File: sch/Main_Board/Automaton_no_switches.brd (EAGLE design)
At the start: 100 x 80 mm, 16 parts, among them IC1 74LS595D, IC2 74LS595D, IC3 74LS595D, IC4 74LS595D, J1 POWER_JACKPTH

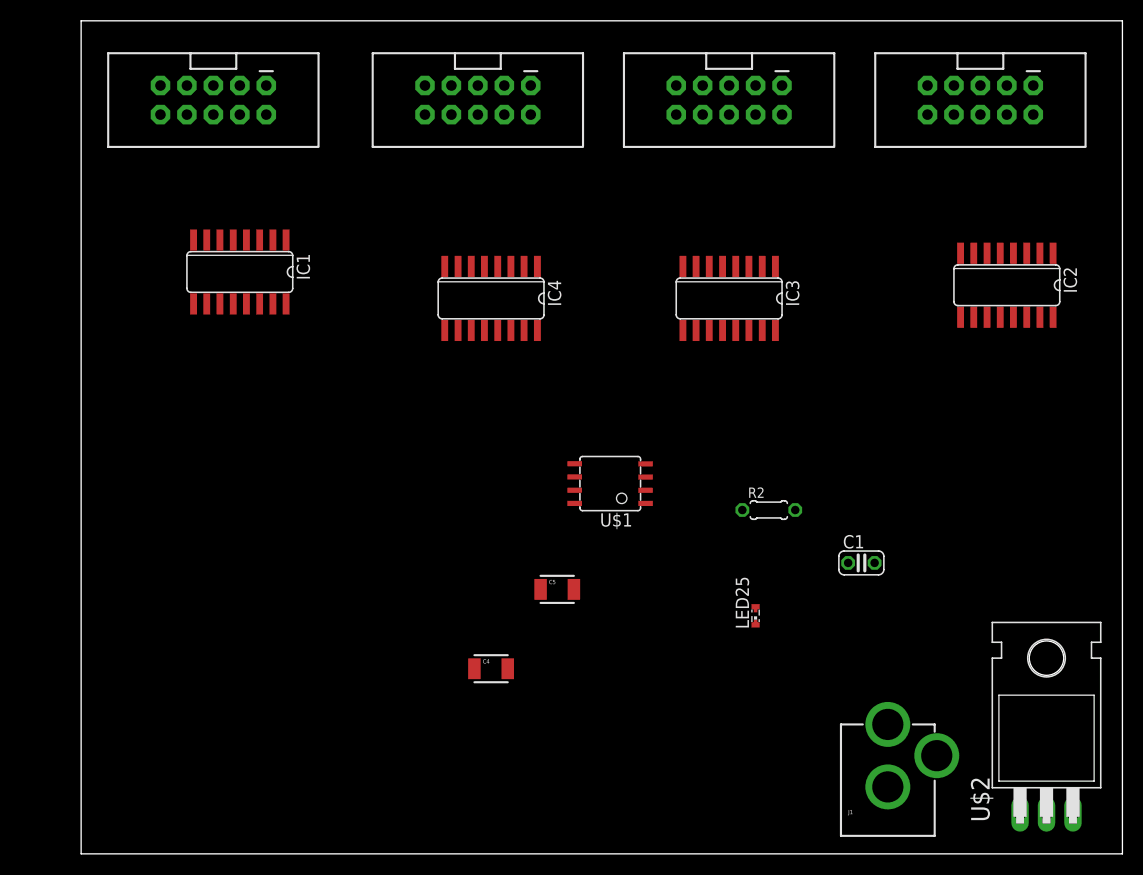
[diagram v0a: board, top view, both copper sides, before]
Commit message: More schematic work.  Make a potentially working board for the main automaton circuit.
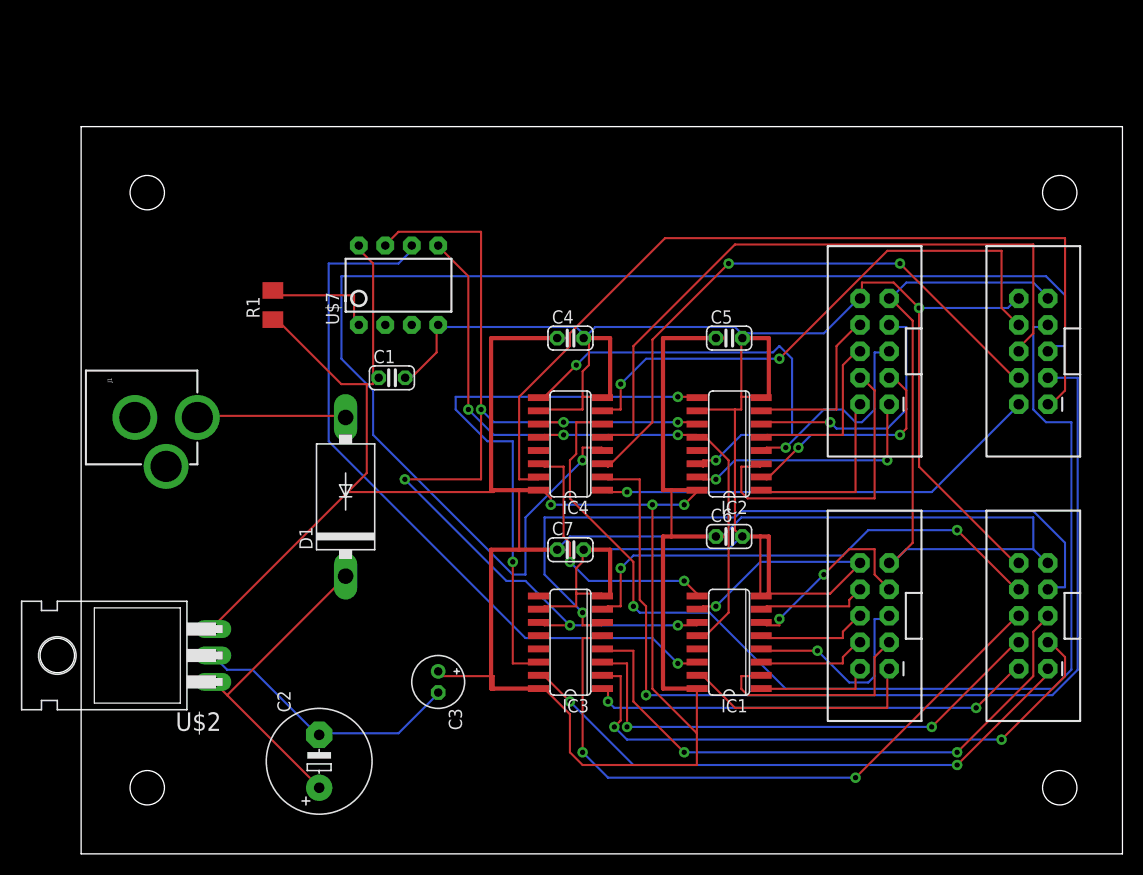
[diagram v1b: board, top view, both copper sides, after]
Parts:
- removed LED25: (no value), led:SMARTLED-TTW
- removed R2: 330, resistor:0204/5
- removed U$1: TINY13-20SU, MyAtmel:8S2
- added C2: 100uf, rcl:E5-10,5
- added C3: 10uf, rcl:E2-5
- added C6, C7: 0.1uf, resistor:C025-024X044
- added D1: 1N5400, diode:DO201-15
- added JP1, JP2, JP3, JP4: STAND-OFF, SparkFun-Electromechanical:STAND-OFF
- added R1: 10k, resistor:M1206
- added U$7: ATTINY85DIP8, *Personal Library:DIP08
- C4: value 10uf -> 0.1uf; device SparkFun:1210 -> resistor:C025-024X044
- C5: value 100uf -> 0.1uf; device SparkFun:1210 -> resistor:C025-024X044
- moved J1 90.9 mm to (-2.54, 41.9), turned to 270 degrees
- moved U$2 90.3 mm to (2.54, 19.1), turned to 90 degrees
- moved U$6 80.5 mm to (76.2, 22.9), turned to 180 degrees
- moved IC1 58.9 mm to (62.2, 20.3), turned to 90 degrees
- moved U$5 58.5 mm to (91.4, 48.3), turned to 180 degrees
- moved U$3 57.5 mm to (91.4, 22.9), turned to 180 degrees
- moved C1 48.5 mm to (29.8, 45.7)
- moved IC3 36.4 mm to (47.0, 20.3), turned to 90 degrees
- moved C4 32.7 mm to (47.0, 49.5)
- moved IC2 30.7 mm to (62.2, 39.4), turned to 90 degrees
- moved C5 29.2 mm to (62.2, 49.5)
- moved U$4 26.2 mm to (76.2, 48.3), turned to 180 degrees
- moved IC4 15.9 mm to (47.0, 39.4), turned to 90 degrees
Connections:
- removed net N$27: LED25.C@1, R2.1
- new net N$2: R1.2, U$7.1
- new net N$3: D1.A, J1.PWR
- net 5V: now also C3.+, C4.1, C5.1, C6.1, C7.1, R1.1, U$7.8; no longer C5.2, LED25.A@1, U$1.1, U$1.8
- net GND: now also C4.2, C5.2, C6.2, C7.2, U$7.4; no longer R2.2, U$1.4
- net LEDS_RCLK: now also U$7.5; no longer U$1.5
- net LEDS_SER: now also U$7.6; no longer U$1.6
- net LEDS_SRCLK: now also U$7.7; no longer U$1.7
- net N$1: now also C2.+, D1.C; no longer C4.2, J1.PWR
- net N$4: now also C2.-, C3.-; no longer C4.1, C5.1
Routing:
- net 5V: track 0.00 -> 292.9 mm
- net GND: track 0.00 -> 230.0 mm, vias 0 -> 2
- net LED_21: track 0.00 -> 130.3 mm, vias 0 -> 1
- net LED_23: track 0.00 -> 106.5 mm, vias 0 -> 1
- net LEDS_SRCLK: track 0.00 -> 101.9 mm, vias 0 -> 6
- net LED_19: track 0.00 -> 98.0 mm, vias 0 -> 1
- net LED_17: track 0.00 -> 86.2 mm
- net LED_7: track 0.00 -> 71.5 mm, vias 0 -> 1
- net LEDS_SER: track 0.00 -> 70.3 mm, vias 0 -> 1
- net VCC: track 0.00 -> 68.2 mm, vias 0 -> 3
- net LEDS_RCLK: track 0.00 -> 65.4 mm, vias 0 -> 3
- net LED_22: track 0.00 -> 64.8 mm
- net LED_6: track 0.00 -> 62.3 mm, vias 0 -> 2
- net LED_5: track 0.00 -> 57.7 mm, vias 0 -> 2
- net LED_20: track 0.00 -> 57.3 mm, vias 0 -> 2
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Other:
- board size 100 x 80 mm -> 100 x 69.8 mm
